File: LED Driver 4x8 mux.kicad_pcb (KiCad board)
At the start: 2 copper layers, 117 x 72.4 mm, 23 parts, among them J1 Barrel_Jack_Switch, J2 Conn_01x02_Female, J3 8P8C_Shielded_x4, Q1 IRF9358TRPBF-2x_p-channel, Q2 IRF9358TRPBF-2x_p-channel, Q3 IRF9358TRPBF-2x_p-channel, Q4 IRF9358TRPBF-2x_p-channel, U1 SN74LV138AT_D_16, U2 TC4468EOE, U3 TC4468EOE

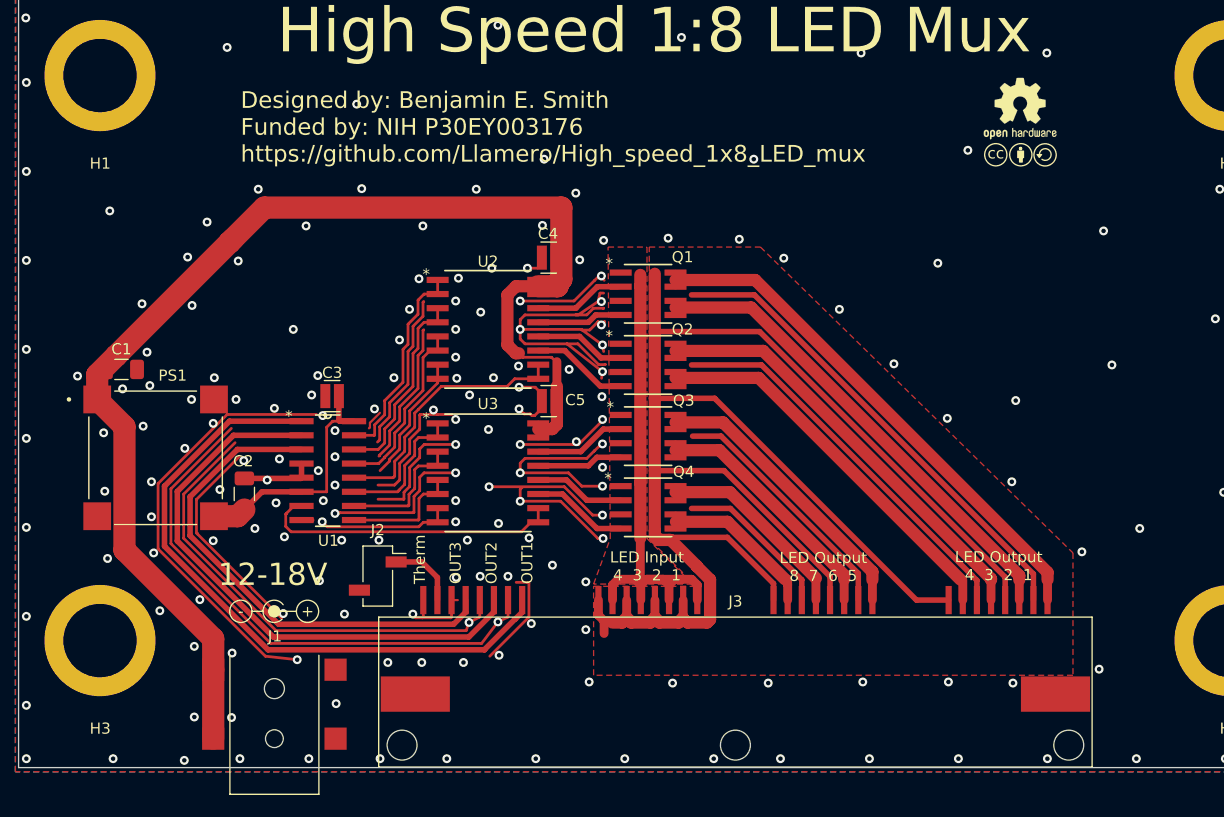
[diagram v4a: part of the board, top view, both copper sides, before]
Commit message: Board powered off LED river backup
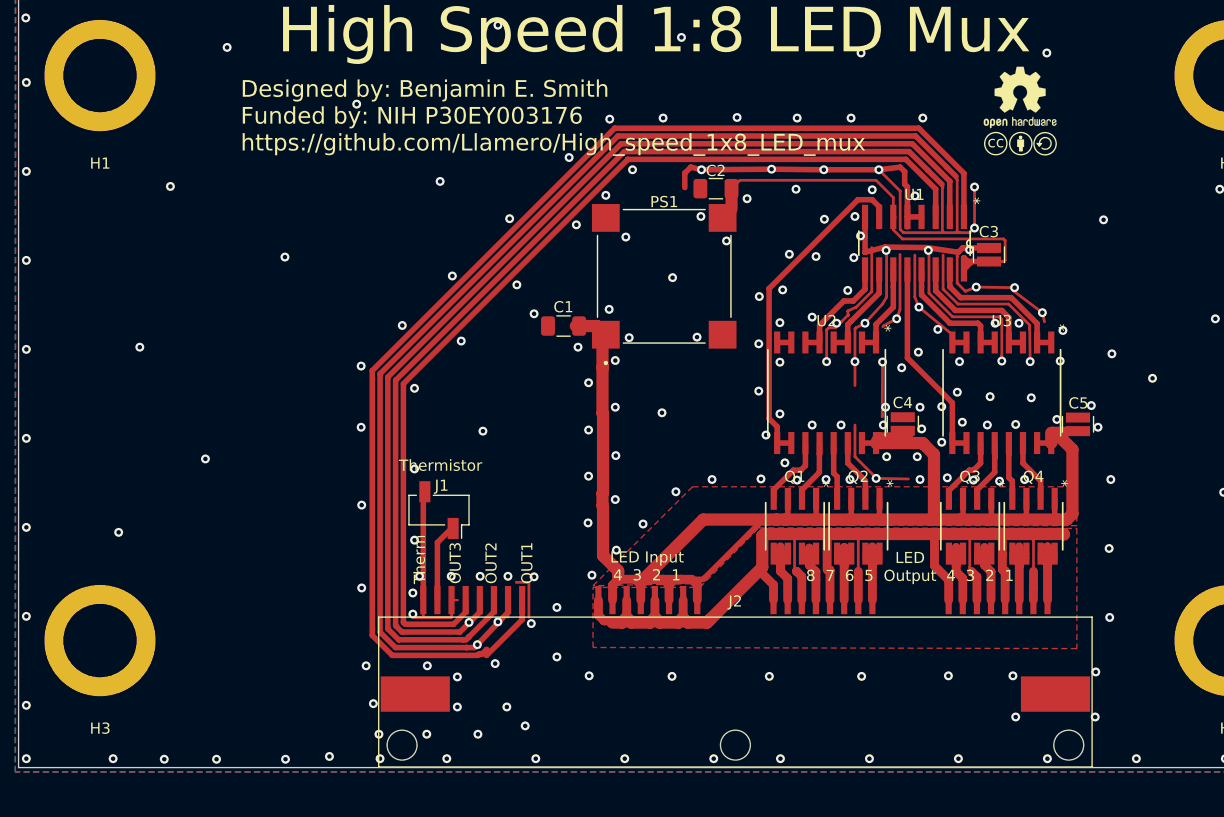
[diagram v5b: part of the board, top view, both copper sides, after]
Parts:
- removed the J2 at (111.8, 142.4)
- removed LOGO2: Jack Polarity, Custom Footprints:Polarity_Center_Positive
- J1: value Barrel_Jack_Switch -> 2 pin header; footprint Custom Footprints:DC-jack_54-00165 -> Connector_PinSocket_2.54mm:PinSocket_1x02_P2.54mm_Vertical_SMD_Pin1Right
- moved C3 60.4 mm to (166.8, 113.5), turned to 270 degrees
- moved U1 56.6 mm to (160.1, 112.5), turned to 270 degrees
- moved C2 50.5 mm to (142.2, 107.5), turned to 180 degrees
- moved PS1 48.6 mm to (137.6, 115.4), turned to 90 degrees
- moved C5 47.6 mm to (174.8, 128.7), turned to 270 degrees
- moved U3 46.6 mm to (167.9, 125.9), turned to 270 degrees
- moved Q4 40.5 mm to (170.8, 137.9), turned to 270 degrees
- moved C1 39.9 mm to (128.5, 119.9), turned to 180 degrees
- moved C4 35.2 mm to (159.0, 128.7), turned to 270 degrees
- moved Q3 32.4 mm to (165.1, 137.9), turned to 270 degrees
- moved U2 31.3 mm to (152.2, 125.9), turned to 270 degrees
- moved J1 29.5 mm to (117.3, 136.4), turned to 270 degrees
- moved Q2 20.6 mm to (155.0, 137.9), turned to 270 degrees
- moved Q1 13.3 mm to (149.3, 137.9), turned to 270 degrees
- moved LOGO1 1.00 mm to (168.4, 102.4)
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- renumbered J3 to J2, Q4 to Q1, Q3 to Q2, Q2 to Q3, Q1 to Q4, U3 to U2, U2 to U3
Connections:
- C1 pad 1: /+18V -> /LED+
- C4 pad 2: /+18V -> /LED+
- C5 pad 2: /+18V -> /LED+
- J1 pad 1: /+18V -> /Thermistor
- PS1 pad 1: /+18V -> /LED+
- U2 pad 15: /+18V -> /LED+
- U2 pad 16: /+18V -> /LED+
- U3 pad 15: /+18V -> /LED+
- U3 pad 16: /+18V -> /LED+
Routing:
- net /LED-: track 286.9 -> 106.6 mm
- net /+18V: track 116.3 -> 0.00 mm
- net /LED+: track 45.2 -> 140.9 mm
- net /OUT1: track 58.7 -> 110.8 mm
- net /OUT2: track 51.8 -> 98.5 mm
- net /OUT3: track 44.9 -> 88.5 mm
- net /LED1+: track 48.1 -> 8.69 mm
- net /LED2+: track 44.4 -> 8.70 mm
- net /LED3+: track 40.0 -> 8.85 mm
- net /LED4+: track 36.2 -> 8.85 mm
- net GND: track 366.1 -> 387.3 mm, vias 211 -> 233
- net /+5V: track 21.8 -> 40.4 mm
- net /LED5+: track 27.1 -> 8.69 mm
- net /LED6+: track 23.3 -> 8.66 mm
- net /LED7+: track 19.0 -> 8.80 mm
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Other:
- board text added: "LED 8 7 6 5 Output 4 3 2 1"
- board text added: "Thermistor"
- board text removed: "12-18V"
- board text removed: "LED Output 4 3 2 1"
- board text removed: "LED Output 8 7 6 5"

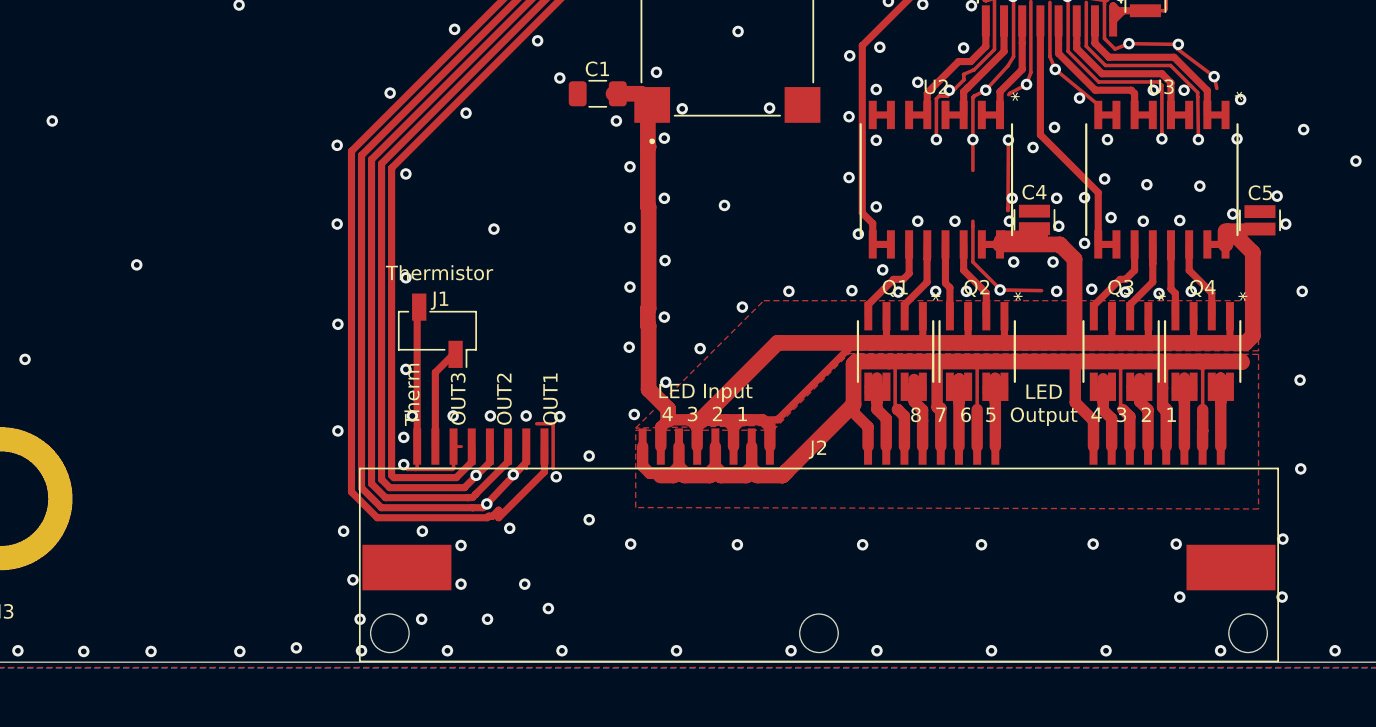
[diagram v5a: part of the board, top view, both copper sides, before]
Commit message: LED driver external power
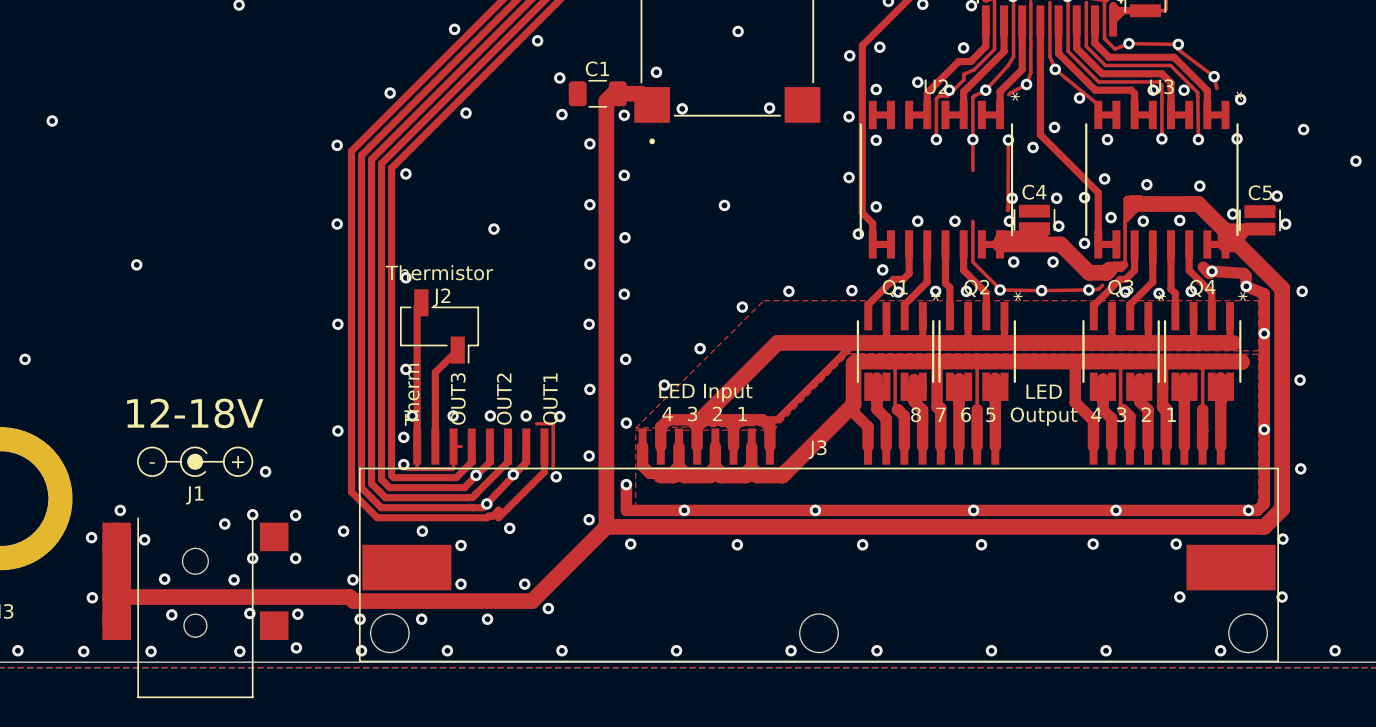
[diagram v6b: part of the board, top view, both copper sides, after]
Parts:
- added J2: Conn_01x02_Female, Connector_PinSocket_2.54mm:PinSocket_1x02_P2.54mm_Vertical_SMD_Pin1Right, F.Cu at (117.5, 136.2)
- added LOGO2: Jack Polarity, Custom Footprints:Polarity_Center_Positive, F.Cu at (100.4, 139.6)
- J1: value 2 pin header -> Barrel_Jack_Switch; footprint Connector_PinSocket_2.54mm:PinSocket_1x02_P2.54mm_Vertical_SMD_Pin1Right -> Custom Footprints:DC-jack_54-00165
- moved J1 30.7 mm to (100.4, 162.1), turned to 90 degrees
- renumbered J2 to J3
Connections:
- C1 pad 1: /LED+ -> /+18V
- C4 pad 2: /LED+ -> /+18V
- C5 pad 2: /LED+ -> /+18V
- J1 pad 1: /Thermistor -> /+18V
- PS1 pad 1: /LED+ -> /+18V
- U2 pad 15: /LED+ -> /+18V
- U2 pad 16: /LED+ -> /+18V
- U3 pad 15: /LED+ -> /+18V
- U3 pad 16: /LED+ -> /+18V
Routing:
- net /+18V: track 0.00 -> 188.8 mm
- net GND: track 387.3 -> 458.3 mm, vias 233 -> 259
- net /LED+: track 140.9 -> 83.0 mm
- net (no net): vias 0 -> 1
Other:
- board text added: "12-18V"

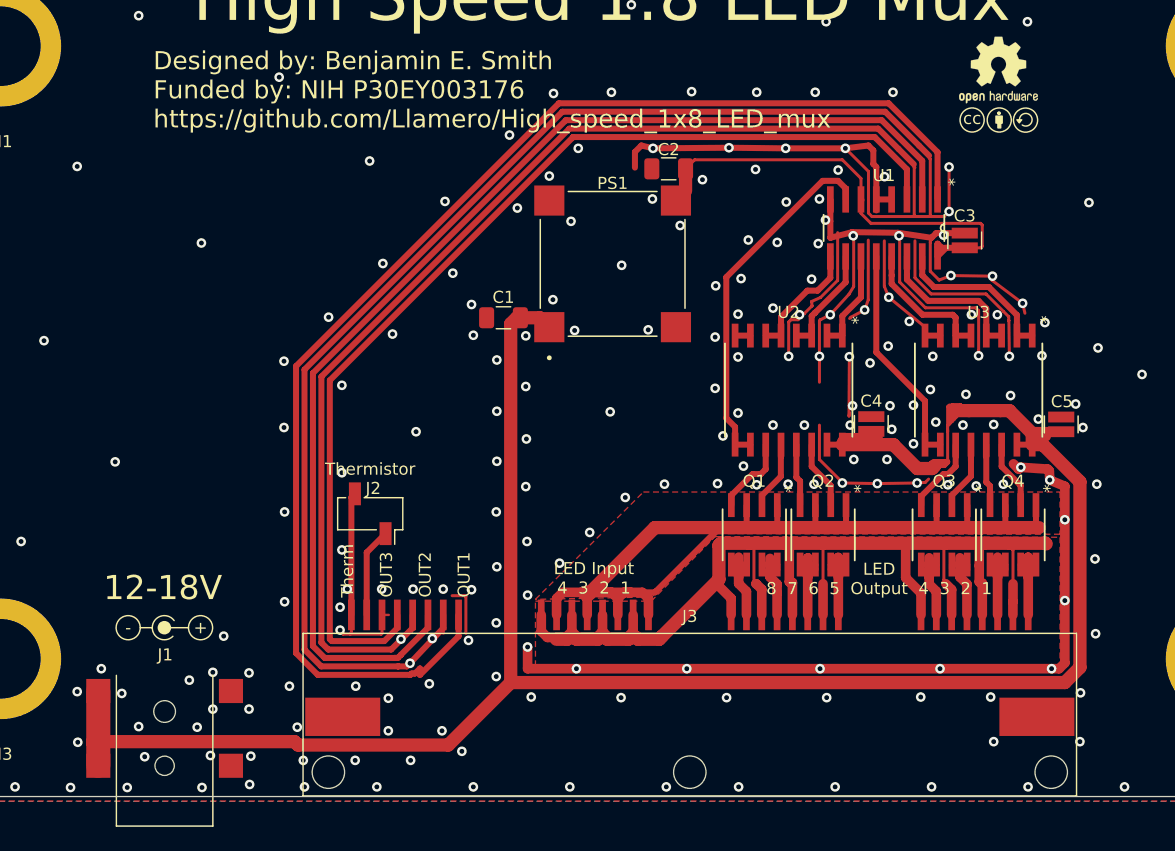
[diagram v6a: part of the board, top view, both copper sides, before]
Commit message: Use Vin through LDO for 5V - no ext. power
This redesign uses an linear regulator to drop the Vin voltage to 5V.  This will greatly reduce the noise on the board, as well as the part count and complexity.
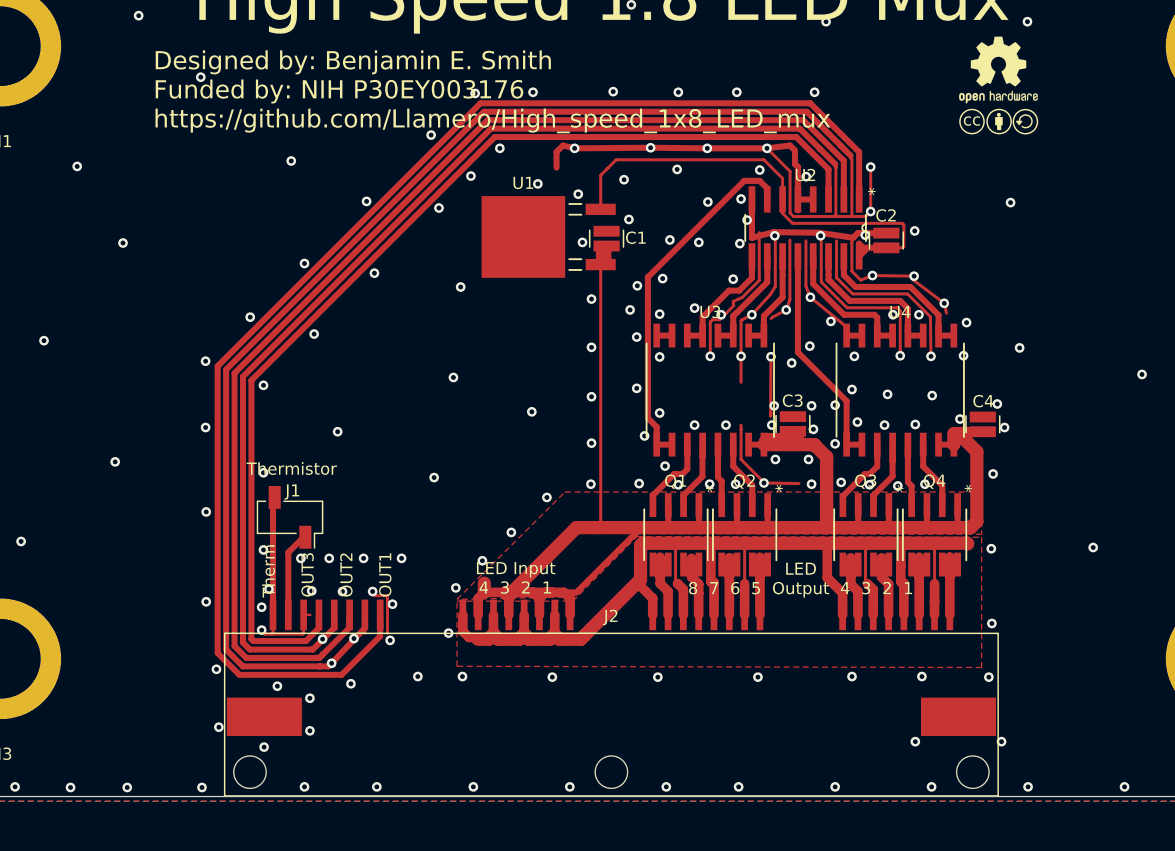
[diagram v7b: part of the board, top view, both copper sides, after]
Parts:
- removed the C2 at (142.2, 107.5)
- removed the J2 at (117.5, 136.2)
- removed LOGO2: Jack Polarity, Custom Footprints:Polarity_Center_Positive
- removed PS1: PXO7805-500-M-TR, Custom Footprints:18V_to_5V_PXO7805-500-M-TR
- added U1: NCV7805BDTRKG, Custom Footprints:12V-5V_lin_reg_NCV7805BDTRKG, F.Cu at (130.2, 113.2)
- C1: value 22µF -> 2.2uF; footprint Capacitor_SMD:C_1206_3216Metric -> Custom Footprints:0508_Capacitor
- J1: value Barrel_Jack_Switch -> 2 pin header; footprint Custom Footprints:DC-jack_54-00165 -> Connector_PinSocket_2.54mm:PinSocket_1x02_P2.54mm_Vertical_SMD_Pin1Right
- Q1, Q2, Q3, Q4: value IRF9358TRPBF-2x_p-channel -> SO8_IRF9358TRPBF_INF
- U3: renamed from U2; value TC4468EOE -> SOIC16-W_MC_MCH
- U4: renamed from U3; value TC4468EOE -> SOIC16-W_MC_MCH
- moved J1 27.6 mm to (110.8, 136.4), turned to 270 degrees
- moved C1 10.8 mm to (137.1, 113.3), turned to 270 degrees
- moved C2 6.50 mm to (160.2, 113.5)
- moved C3 6.50 mm to (152.5, 128.7)
- moved C4 6.50 mm to (168.2, 128.7)
- moved J2 6.50 mm to (137.4, 143.3)
- moved Q1 6.50 mm to (142.8, 137.9)
- moved Q2 6.50 mm to (148.5, 137.9)
- moved Q3 6.50 mm to (158.6, 137.9)
- moved Q4 6.50 mm to (164.2, 137.9)
- moved U2 6.50 mm to (153.6, 112.5)
- moved U3 6.50 mm to (145.7, 125.9)
- moved U4 6.50 mm to (161.4, 125.9)
- moved LOGO1 0.13 mm to (168.3, 102.5)
- renumbered C3 to C2, C4 to C3, C5 to C4, J3 to J2, U1 to U2
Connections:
- C1 pad 1: /+18V -> GND
- C1 pad 2: GND -> /LED+
- C3 pad 2: /+18V -> /LED+
- C4 pad 2: /+18V -> /LED+
- J1 pad 1: /+18V -> /Thermistor
- U3 pad 15: /+18V -> /LED+
- U3 pad 16: /+18V -> /LED+
- U4 pad 15: /+18V -> /LED+
- U4 pad 16: /+18V -> /LED+
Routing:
- net /+18V: track 188.8 -> 0.00 mm
- net GND: track 458.3 -> 387.3 mm, vias 259 -> 229
- net /LED+: track 83.0 -> 141.2 mm
- net /+5V: track 40.4 -> 41.2 mm
- net /OUT1: track 110.8 -> 110.0 mm
- net (no net): vias 1 -> 0
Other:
- board text removed: "12-18V"
